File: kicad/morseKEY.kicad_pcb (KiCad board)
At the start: 2 copper layers, 50.8 x 17.8 mm, 16 parts, among them P1 USB_A, P2 KEY, P3 ISP, U1 ATTINY85-P

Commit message: board layout
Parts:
- C1: footprint Capacitors_ThroughHole:C_Disc_D3_P2.5 -> morseKEY:C_Disc_D3_P2.5
- C2: footprint Capacitors_ThroughHole:C_Radial_D5_L6_P2.5 -> morseKEY:C_Radial_D5_L6_P2.5
- D1, D2: footprint Diodes_ThroughHole:Diode_DO-35_SOD27_Horizontal_RM10 -> morseKEY:Diode_DO-41_SOD81_Vertical_KathodeUp
- P1: footprint Connect:USB_A -> morseKEY:USB_A
- P2: footprint Pin_Headers:Pin_Header_Straight_1x03 -> morseKEY:Pin_Header_Straight_1x03
- P3: footprint Pin_Headers:Pin_Header_Straight_2x03 -> morseKEY:Pin_Header_Straight_2x03
- R1, R2, R3: footprint Resistors_ThroughHole:Resistor_Horizontal_RM10mm -> morseKEY:Resistor_Vertical_RM5mm
- R4: value 2k2 -> 2k5; footprint Pin_Headers:Pin_Header_Straight_1x03 -> morseKEY:Pin_Header_Straight_1x03
- R5: value 2k2 -> 2k5; footprint Resistors_ThroughHole:Resistor_Horizontal_RM10mm -> morseKEY:Resistor_Vertical_RM5mm
- SP1: footprint Pin_Headers:Pin_Header_Straight_1x02 -> morseKEY:Pin_Header_Straight_1x04
- U1: footprint Housings_DIP:DIP-8_W7.62mm_LongPads -> morseKEY:DIP-8_W7.62mm_LongPads
- moved SP1 7.96 mm to (153.0, 111.1), turned to 90 degrees
- moved P3 7.43 mm to (148.0, 111.1)
- moved R4 7.41 mm to (142.2, 111.1), turned to 0 degrees
- moved P2 6.84 mm to (157.5, 111.1)
- moved R3 6.73 mm to (120.0, 117.7)
- moved R5 6.62 mm to (139.7, 117.5), turned to 180 degrees
- moved U1 5.39 mm to (134.0, 109.9)
- moved C2 4.96 mm to (127.5, 117.2)
- moved D1 4.44 mm to (122.3, 107.8)
- moved D2 4.13 mm to (122.3, 114.4)
- moved R2 2.84 mm to (120.0, 111.1)
- moved R1 1.63 mm to (120.0, 104.5)
- moved C1 0.90 mm to (132.8, 117.2)
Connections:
- SP1 pad 2: /GND -> /MISO
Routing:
- net /GND: track 0.00 -> 109.6 mm
- net /5V: track 0.00 -> 70.5 mm
- net /MOSI: track 0.00 -> 41.8 mm
- net /SCK: track 0.00 -> 39.2 mm
- net /MISO: track 0.00 -> 35.2 mm
- net /K3: track 0.00 -> 30.3 mm
- net /K1: track 0.00 -> 24.1 mm
- net /RST: track 0.00 -> 21.7 mm
- net /D+: track 0.00 -> 17.0 mm
- net /D-: track 0.00 -> 16.8 mm
- added copper zone on F.Cu, net /5V
- added copper zone on B.Cu, net /GND
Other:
- net class 0.5 added: clearance 0.2, trace_width 0.5, via_dia 0.6, via_drill 0.4
- net class 0.75 added: clearance 0.2, trace_width 0.75, via_dia 0.6, via_drill 0.4
- net class 1.0 added: clearance 0.2, trace_width 1, via_dia 0.6, via_drill 0.4

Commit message: 3D render
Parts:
- R4: footprint morseKEY:Pin_Header_Straight_1x03 -> morseKEY:res_vert

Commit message: board layout
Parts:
- added G***: LOGO, morseKEY:morseKEY, B.Cu at (56.1, 34.8)
- added G***: LOGO, morseKEY:OSHW_logo_notext, F.Cu at (72.4, 41.3)
- D1, D2: footprint morseKEY:Diode_DO-41_SOD81_Vertical_KathodeUp -> morseKEY:Diode_DO-41_SOD81_Vertical_KathodeUp_2
- P1: footprint morseKEY:USB_A -> morseKEY:USB_A_up2-ah-th
- moved P1 107.9 mm to (33.0, 35.6)
- moved C1 106.9 mm to (57.3, 41.7)
- moved C2 106.9 mm to (51.9, 41.7)
- moved D1 106.9 mm to (46.7, 32.3)
- moved D2 106.9 mm to (46.7, 38.9)
- moved P3 106.9 mm to (72.4, 35.6)
- moved R1 106.9 mm to (44.5, 29.0)
- moved R2 106.9 mm to (44.5, 35.6)
- moved R3 106.9 mm to (44.5, 42.2)
- moved R4 106.9 mm to (66.7, 35.6)
- moved R5 106.9 mm to (64.2, 41.9)
- moved REF** 106.9 mm to (81.3, 41.9)
- moved REF** 106.9 mm to (81.3, 29.2)
- moved SP1 106.9 mm to (77.5, 35.6)
- moved U1 106.9 mm to (58.4, 34.3)
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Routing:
- net /GND: track 109.6 -> 104.2 mm
- net /5V: track 70.5 -> 69.9 mm
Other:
- board text added: "OpenSource Hardware"

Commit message: gerbers
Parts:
- removed G***: LOGO, morseKEY:morseKEY
- removed REF** (x2): 1pin, Connect:1pin
- added G2: CKT, morseKEY:morseKEY, B.Cu at (49.5, 32.4)
- added P4: MTG, morseKEY:1pin, F.Cu at (74.0, 27.6)
- added P5: MTG, morseKEY:1pin, F.Cu at (74.0, 38.5)
- G1: renamed from G***; value LOGO -> OSHW-LOGO
- moved D2 9.84 mm to (37.5, 35.6), turned to 0 degrees
- moved C2 9.46 mm to (43.2, 38.1)
- moved D1 9.44 mm to (37.5, 30.5), turned to 0 degrees
- moved R3 9.20 mm to (36.2, 38.1)
- moved P3 9.16 mm to (64.8, 30.5), turned to 180 degrees
- moved R2 8.64 mm to (36.2, 33.0)
- moved R4 8.52 mm to (59.1, 31.8)
- moved R1 8.32 mm to (36.2, 27.9)
- moved G1 8.26 mm to (64.8, 38.1), turned to 90 degrees
- moved P1 8.03 mm to (25.4, 33.0)
- moved P2 8.03 mm to (74.3, 33.0)
- moved SP1 8.03 mm to (69.8, 33.0)
- moved U1 8.03 mm to (50.8, 31.8)
- moved R5 6.90 mm to (58.4, 38.1)
- moved C1 6.87 mm to (50.8, 39.4)
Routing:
- net /5V: track 69.9 -> 60.0 mm
- net /D+: track 16.7 -> 8.97 mm
- net /K1: track 24.1 -> 30.0 mm
- net /MOSI: track 41.8 -> 36.4 mm
- net /D-: track 16.4 -> 12.0 mm
- net /RST: track 21.7 -> 25.1 mm
- net /SCK: track 39.2 -> 41.9 mm
- net /GND: track 104.2 -> 104.8 mm
- removed copper zone on F.Cu, net /5V
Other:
- board size 50.8 x 17.8 mm -> 50.8 x 15.2 mm
- board text added: "forked from : mitxela.com/projects/morse_code_usb_keyboard_mk_ii"
- board text added: "morseKEY"
- board text added: "wyolum.com github.com/wyolum"

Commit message: BoM
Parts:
- R4: value 2k5 -> 1k5
- R5: value 2k5 -> 3k3
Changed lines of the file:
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@@
     (links 38)
     (no_connects 0)
-    (area 10.199999 23.536 88.007144 47.15)
+    (area 25.324999 25.324999 76.275001 40.715001)
     (thickness 1.6)
     (drawings 44)
@@
     (pad_to_mask_clearance 0.2)
     (aux_axis_origin 0 0)
-    (visible_elements FFFFEFFF)
+    (visible_elements FFFFFF7F)
     (pcbplotparams
       (layerselection 0x00030_00000000)
@@
     (pad 6 thru_hole rect (at 1.27 2.54 180) (size 1.7272 1.7272) (drill 1.016) (layers *.Cu *.Mask F.SilkS)
       (net 2 /GND))
-    (model header_2x3_TH_2_54mm.wrl
-      (at (xyz 0 0 0))
-      (scale (xyz 1 1 1))
-      (rotate (xyz 0 0 90))
-    )
   )
   (module morseKEY:C_Radial_D5_L6_P2.5 (layer F.Cu)
@@
     (pad 4 thru_hole rect (at 3.81 0 90) (size 1.651 2.286) (drill 1.016) (layers *.Cu *.Mask F.SilkS)
       (net 2 /GND))
-    (model header_1x4_TH_2_54mm.wrl
+    (model PS1240P02BT.wrl
       (at (xyz 0 0 0))
       (scale (xyz 1 1 1))
@@
     (pad 3 thru_hole oval (at 0 2.54) (size 2.286 1.651) (drill 1.016) (layers *.Cu *.Mask F.SilkS)
       (net 6 /K3))
-    (model header_1x3_TH_2_54mm.wrl
+    (model header_Male_RA_Low_3Pin.wrl
       (at (xyz 0 0 0))
       (scale (xyz 1 1 1))
@@
       (effects (font (size 0.762 0.762) (thickness 0.127)))
     )
-    (fp_text value 2k5 (at 0 -5.64) (layer F.Fab) hide
+    (fp_text value 1k5 (at 0 -5.64) (layer F.Fab) hide
       (effects (font (size 0.762 0.762) (thickness 0.127)))
     )
@@
       (effects (font (size 0.762 0.762) (thickness 0.127)))
     )
-    (fp_text value 2k5 (at -2.54 0.254 180) (layer F.SilkS) hide
-      (effects (font (size 0.762 0.762) (thickness 0.127)))
-    )
+    (fp_text value 3k3 (at -2.54 0.254 180) (layer F.SilkS) hide
+      (effects (font (size 0.762 0.762) (thickness 0.127)))
+    )

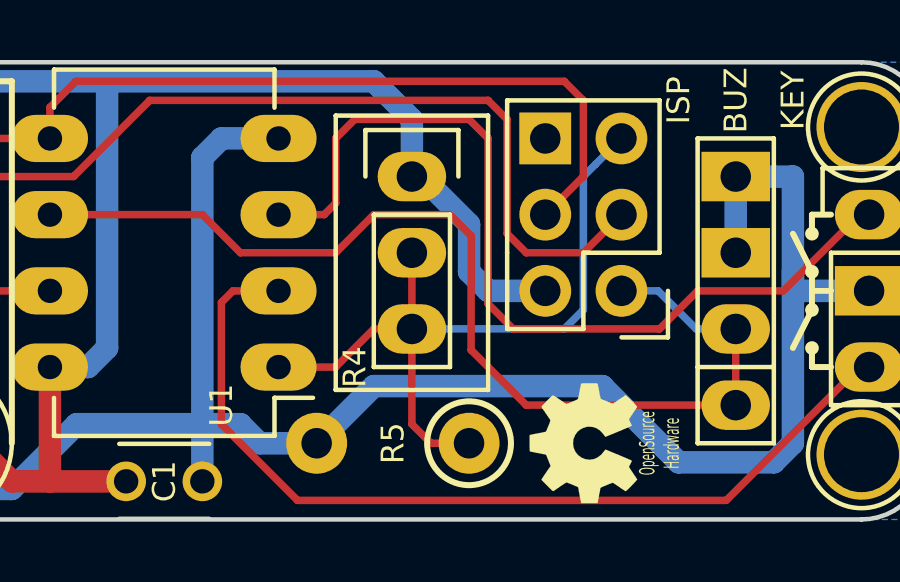
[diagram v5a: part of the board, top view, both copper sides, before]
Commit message: changed RST resistor divider
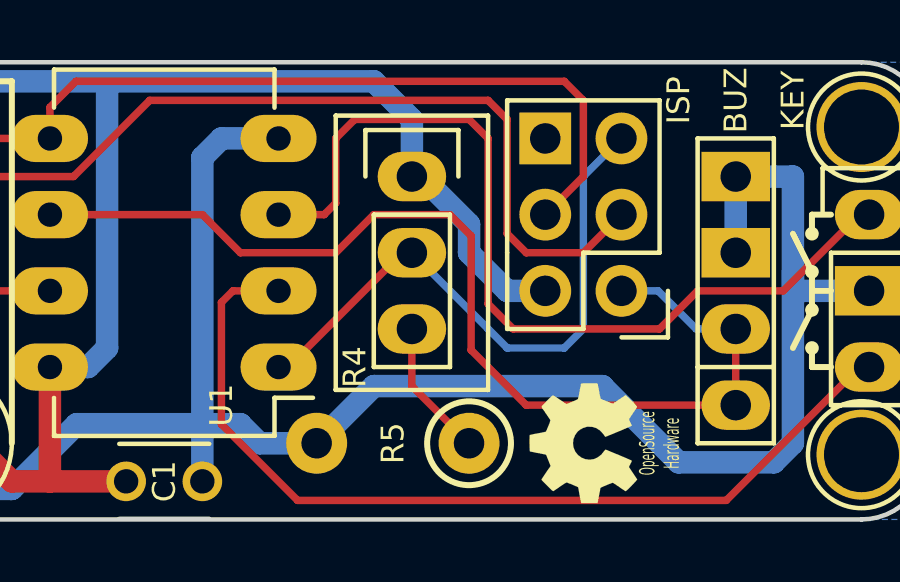
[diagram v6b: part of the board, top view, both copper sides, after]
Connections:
- R4 pad 3: /RST -> Net-(R4-Pad3)
- R5 pad 1: /RST -> Net-(R4-Pad3)
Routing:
- net /RST: track 25.1 -> 20.2 mm
- net Net-(R4-Pad3): track 0.00 -> 4.60 mm
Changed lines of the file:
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@@
 (kicad_pcb (version 4) (host pcbnew 4.0.5-e0-6337~49~ubuntu16.04.1)
   (general
-    (links 38)
+    (links 37)
     (no_connects 0)
-    (area 25.324999 25.324999 76.275001 40.715001)
+    (area 10.199999 23.536 88.007144 47.15)
     (thickness 1.6)
     (drawings 44)
-    (tracks 134)
+    (tracks 133)
     (zones 0)
     (modules 18)
-    (nets 11)
+    (nets 12)
   )
   (page A4)
@@
     (visible_elements FFFFFF7F)
     (pcbplotparams
-      (layerselection 0x00030_00000000)
+      (layerselection 0x010f0_80000001)
       (usegerberextensions true)
       (usegerberattributes true)
@@
   (net 9 /MOSI)
   (net 10 /RST)
+  (net 11 "Net-(R4-Pad3)")
   (net_class Default "This is the default net class."
     (clearance 0.2)
@@
     (add_net /RST)
     (add_net /SCK)
+    (add_net "Net-(R4-Pad3)")
   )
   (net_class 0.5 ""
@@
       (net 10 /RST))
     (pad 3 thru_hole oval (at 0 2.54) (size 2.286 1.651) (drill 1.016) (layers *.Cu *.Mask F.SilkS)
-      (net 10 /RST))
+      (net 11 "Net-(R4-Pad3)"))
     (model trimpot_vert.wrl
       (at (xyz 0 0 0))
@@
     (fp_circle (center -2.54 0) (end -1.143 0) (layer F.SilkS) (width 0.2))
     (pad 1 thru_hole circle (at -2.54 0 180) (size 2.032 2.032) (drill 1.016) (layers *.Cu *.SilkS *.Mask)
-      (net 10 /RST))
+      (net 11 "Net-(R4-Pad3)"))
     (pad 2 thru_hole circle (at 2.54 0 180) (size 2.032 2.032) (drill 1.016) (layers *.Cu *.SilkS *.Mask)
       (net 2 /GND))
@@
   (gr_line (start 76.2 27.559) (end 76.2 38.481) (angle 90) (layer Edge.Cuts) (width 0.15))
   (gr_line (start 27.305 25.4) (end 74.041 25.4) (angle 90) (layer Edge.Cuts) (width 0.15))
-  (segment (start 63.5 33.02) (end 61.595 33.02) (width 0.75) (layer B.Cu) (net 1))
-  (segment (start 60.96 32.385) (end 60.96 30.7975) (width 0.75) (layer B.Cu) (net 1))
-  (segment (start 61.595 33.02) (end 60.96 32.385) (width 0.75) (layer B.Cu) (net 1))
+  (segment (start 63.5 33.02) (end 62.23 33.02) (width 0.75) (layer B.Cu) (net 1))
+  (segment (start 60.96 31.75) (end 60.96 30.7975) (width 0.75) (layer B.Cu) (net 1))
+  (segment (start 62.23 33.02) (end 60.96 31.75) (width 0.75) (layer B.Cu) (net 1))
   (segment (start 59.3725 29.21) (end 59.055 29.21) (width 0.75) (layer B.Cu) (net 1))
   (segment (start 60.96 30.7975) (end 59.3725 29.21) (width 0.75) (layer B.Cu) (net 1))
@@
   (segment (start 43.18 27.94) (end 42.545 28.575) (width 0.25) (layer F.Cu) (net 9))
   (segment (start 46.99 27.94) (end 43.18 27.94) (width 0.25) (layer F.Cu) (net 9) (status 10))
-  (segment (start 64.77 33.655) (end 64.77 29.21) (width 0.25) (layer B.Cu) (net 10))
-  (segment (start 64.135 34.29) (end 64.77 33.655) (width 0.25) (layer B.Cu) (net 10))
-  (segment (start 59.055 34.29) (end 64.135 34.29) (width 0.25) (layer B.Cu) (net 10))
-  (segment (start 65.176401 28.803599) (end 66.04 27.94) (width 0.25) (layer B.Cu) (net 10))
-  (segment (start 64.77 29.21) (end 65.176401 28.803599) (width 0.25) (layer B.Cu) (net 10))
-  (segment (start 54.61 35.56) (end 56.515 35.56) (width 0.25) (layer F.Cu) (net 10))
-  (segment (start 56.515 35.56) (end 57.785 34.29) (width 0.25) (layer F.Cu) (net 10))
-  (segment (start 57.785 34.29) (end 59.055 34.29) (width 0.25) (layer F.Cu) (net 10))
-  (segment (start 59.055 34.29) (end 59.055 37.465) (width 0.25) (layer F.Cu) (net 10) (status 10))
-  (segment (start 59.69 38.1) (end 60.96 38.1) (width 0.25) (layer F.Cu) (net 10))
-  (segment (start 59.055 37.465) (end 59.69 38.1) (width 0.25) (layer F.Cu) (net 10))
-  (segment (start 59.055 31.75) (end 59.055 34.29) (width 0.25) (layer F.Cu) (net 10) (status 30))
+  (segment (start 66.04 27.94) (end 64.77 29.21) (width 0.25) (layer B.Cu) (net 10))
+  (segment (start 64.77 29.21) (end 64.77 34.29) (width 0.25) (layer B.Cu) (net 10))
+  (segment (start 64.77 34.29) (end 64.135 34.925) (width 0.25) (layer B.Cu) (net 10))
+  (segment (start 64.135 34.925) (end 62.23 34.925) (width 0.25) (layer B.Cu) (net 10))
+  (segment (start 62.23 34.925) (end 61.595 34.29) (width 0.25) (layer B.Cu) (net 10))
+  (segment (start 61.595 34.29) (end 59.055 31.75) (width 0.25) (layer B.Cu) (net 10))
+  (segment (start 59.055 31.75) (end 58.7375 31.75) (width 0.25) (layer F.Cu) (net 10))
+  (segment (start 58.7375 31.75) (end 54.9275 35.56) (width 0.25) (layer F.Cu) (net 10))
+  (segment (start 54.9275 35.56) (end 54.61 35.56) (width 0.25) (layer F.Cu) (net 10))
+  (segment (start 59.055 34.29) (end 59.055 36.195) (width 0.25) (layer F.Cu) (net 11))
+  (segment (start 59.055 36.195) (end 60.96 38.1) (width 0.25) (layer F.Cu) (net 11))
   (zone (net 2) (net_name /GND) (layer B.Cu) (hatch edge 0.508)
     (connect_pads (clearance 0.381))

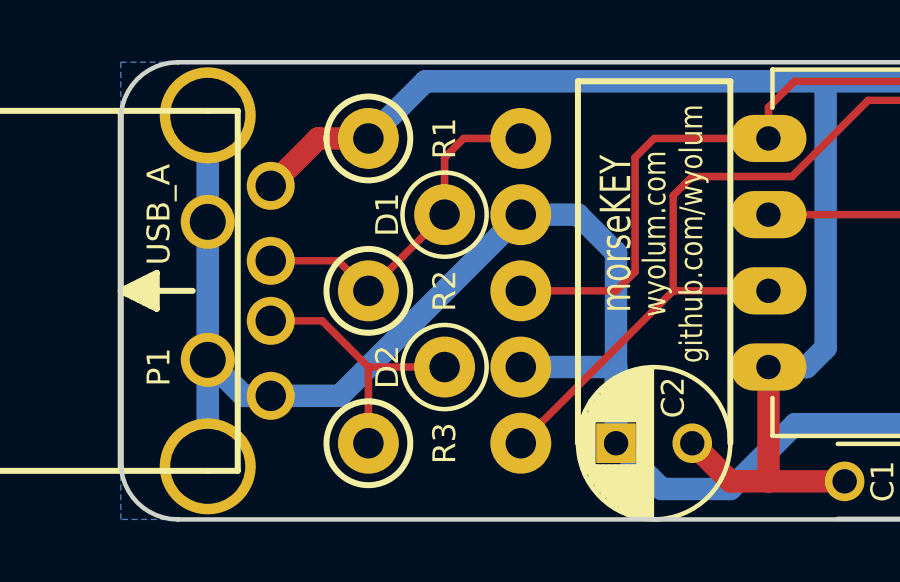
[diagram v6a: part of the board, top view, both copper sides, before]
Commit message: reverse pinout of USB connector, reroute
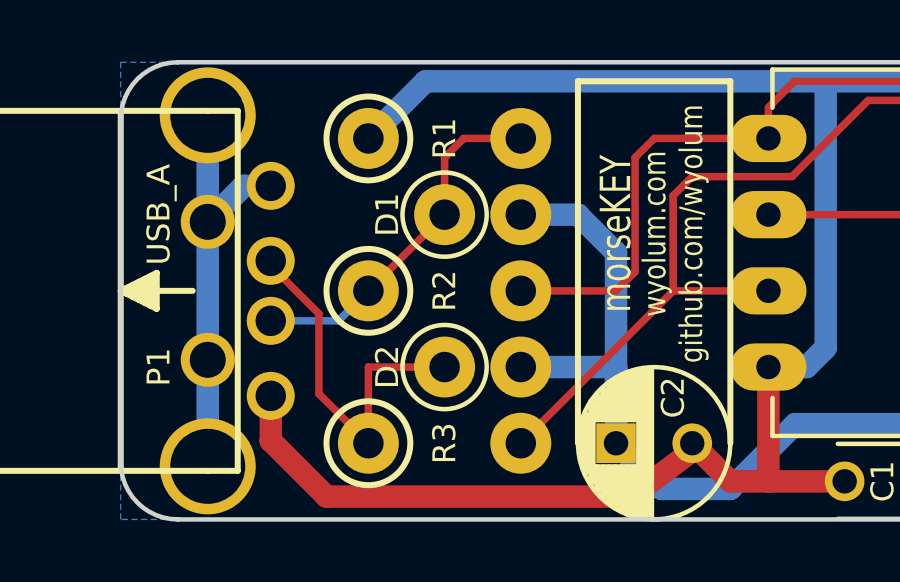
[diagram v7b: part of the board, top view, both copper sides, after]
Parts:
- P1: footprint morseKEY:USB_A_up2-ah-th -> USB_A_up2-ah-th
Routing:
- net /5V: track 59.6 -> 72.8 mm
- net /GND: track 104.8 -> 93.9 mm
- net /D+: track 8.97 -> 12.5 mm

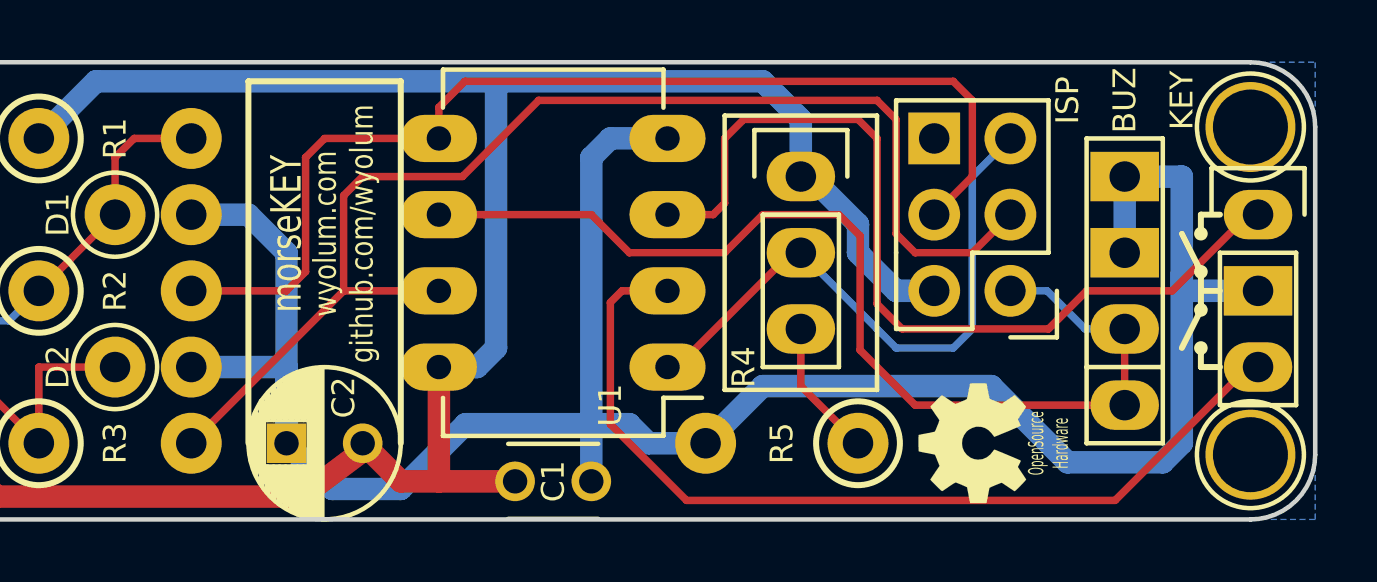
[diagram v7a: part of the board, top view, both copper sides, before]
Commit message: morseKEY update for KiCad FreeCAD demo tutorial
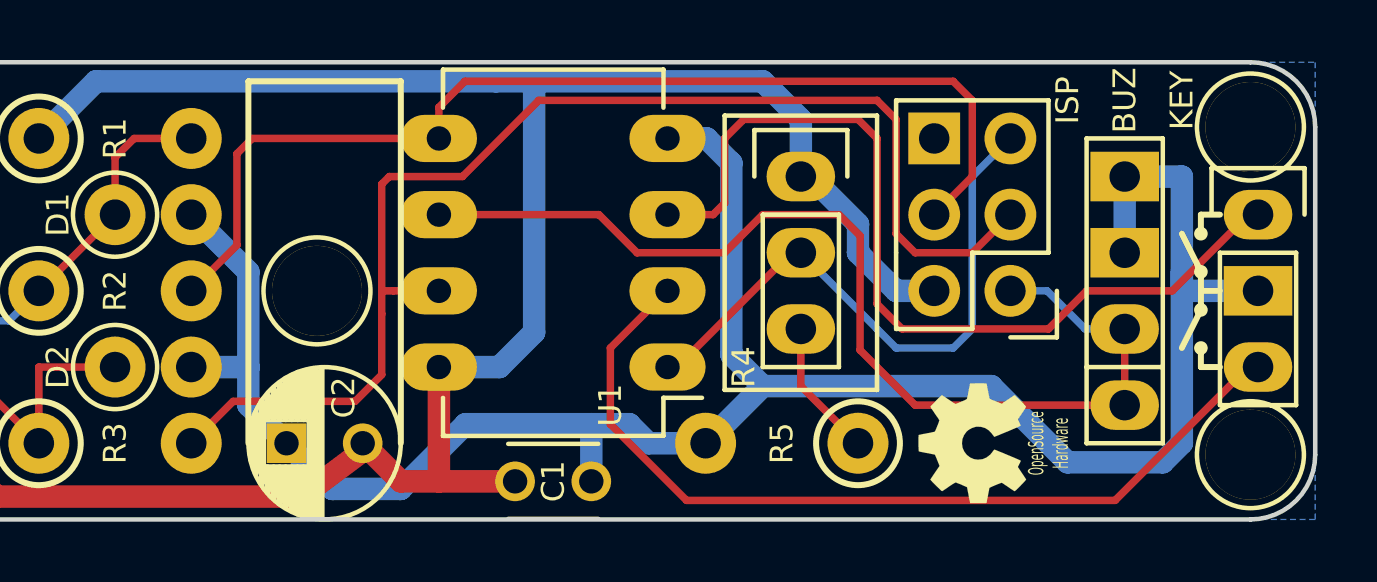
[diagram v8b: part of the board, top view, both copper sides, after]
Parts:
- removed G2: CKT, morseKEY:morseKEY
- added P6: MTG, morseKEY:1pin, F.Cu at (42.9, 33.0)
- P1: footprint USB_A_up2-ah-th -> morseKEY:USB_A_up2-ah-th
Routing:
- net /GND: track 93.9 -> 87.6 mm
- net /5V: track 72.8 -> 73.7 mm
- net /K3: track 30.6 -> 29.7 mm
- net /SCK: track 41.9 -> 42.5 mm
